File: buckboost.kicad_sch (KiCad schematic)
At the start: 25 parts, among them Q3 DUAL_N_FET, Q4 DUAL_N_FET, U4 LM5176

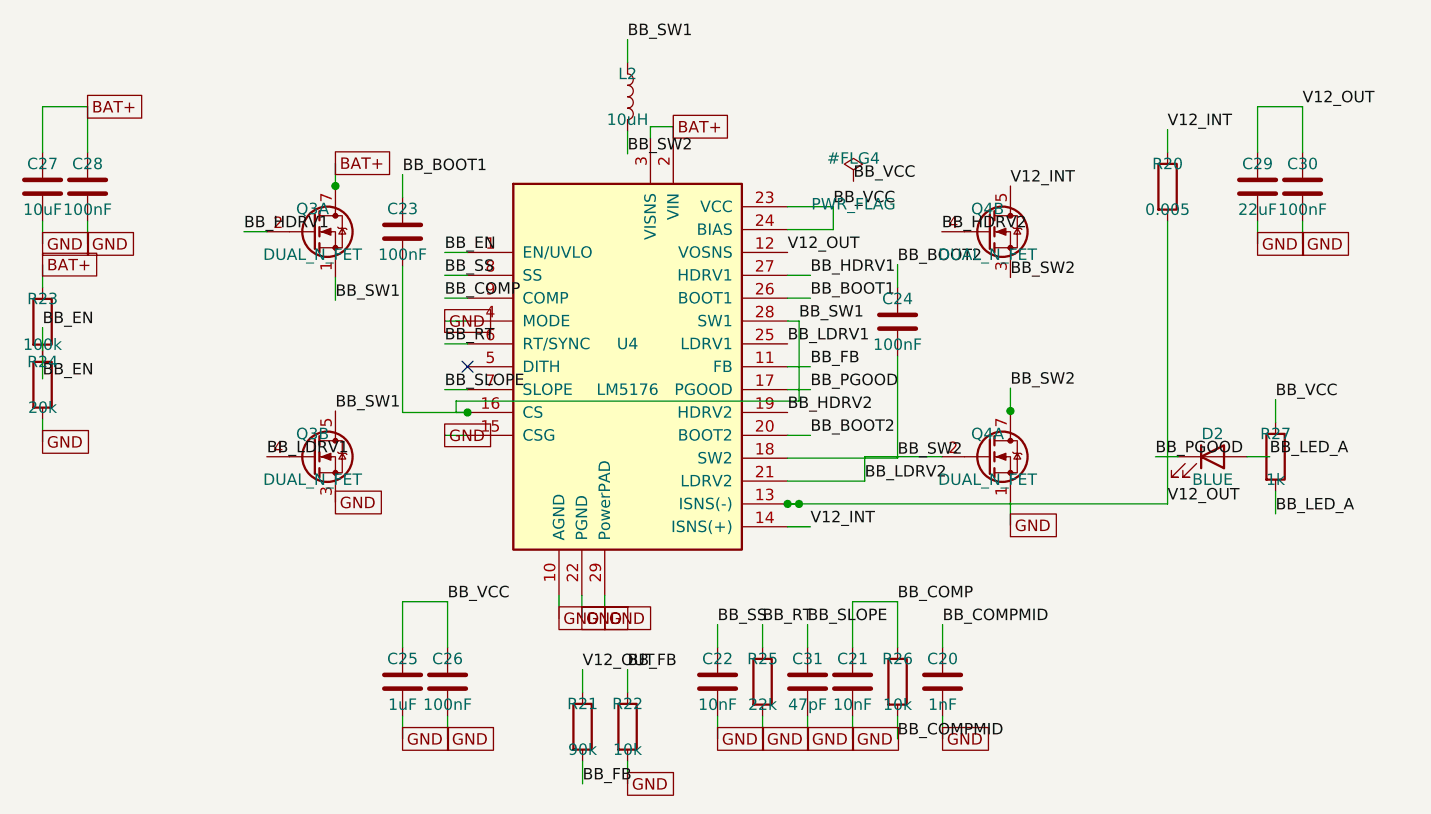
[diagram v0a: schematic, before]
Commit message: schematic: integrate subcircuits — output, I²C, user switch
Top-level power_module.kicad_sch gains the user-facing components:

  J2  Conn_01x02   output header        : V12_OUT, GND
  J3  Conn_01x04   I²C breakout         : SDA, SCL, ALERT, GND
  SW1 SW_SPDT      user on/off switch   : MODULE_EN ↔ BAT+ (pin 3 NC)

For these to span sheets, V12_OUT (Buck-Boost) and SDA/SCL/ALERT (BMS)
were promoted from local labels to global_label inside their child
sheets (one Python pass over each .kicad_sch).  KiCad joins
global_labels by name across all sheets without sheet pins.

User switch behaviour: SW1 routes BAT+ through to a new MODULE_EN
global net.  Inside buckboost.kicad_sch, R23.pin1 (top of the
LM5176 EN/UVLO divider) was switched from BAT+ to MODULE_EN — so
opening SW1 lets R24 pull EN/UVLO low and the buck-boost shuts
down (BMS still runs at its ~10 µA sleep current).

Cleanup: SW1 placeholder in the BMS sheet was deleted (it was
intentionally unwired pending integration; now the real user switch
lives at the parent).

ERC: top-level reports zero errors.  One warning remains
(L_Bourns_SRR1280 footprint not found in default library — pending
the LCSC/footprint-property pass that's still on the to-do list).

Co-Authored-By: Claude Opus 4.7 <noreply@anthropic.com>
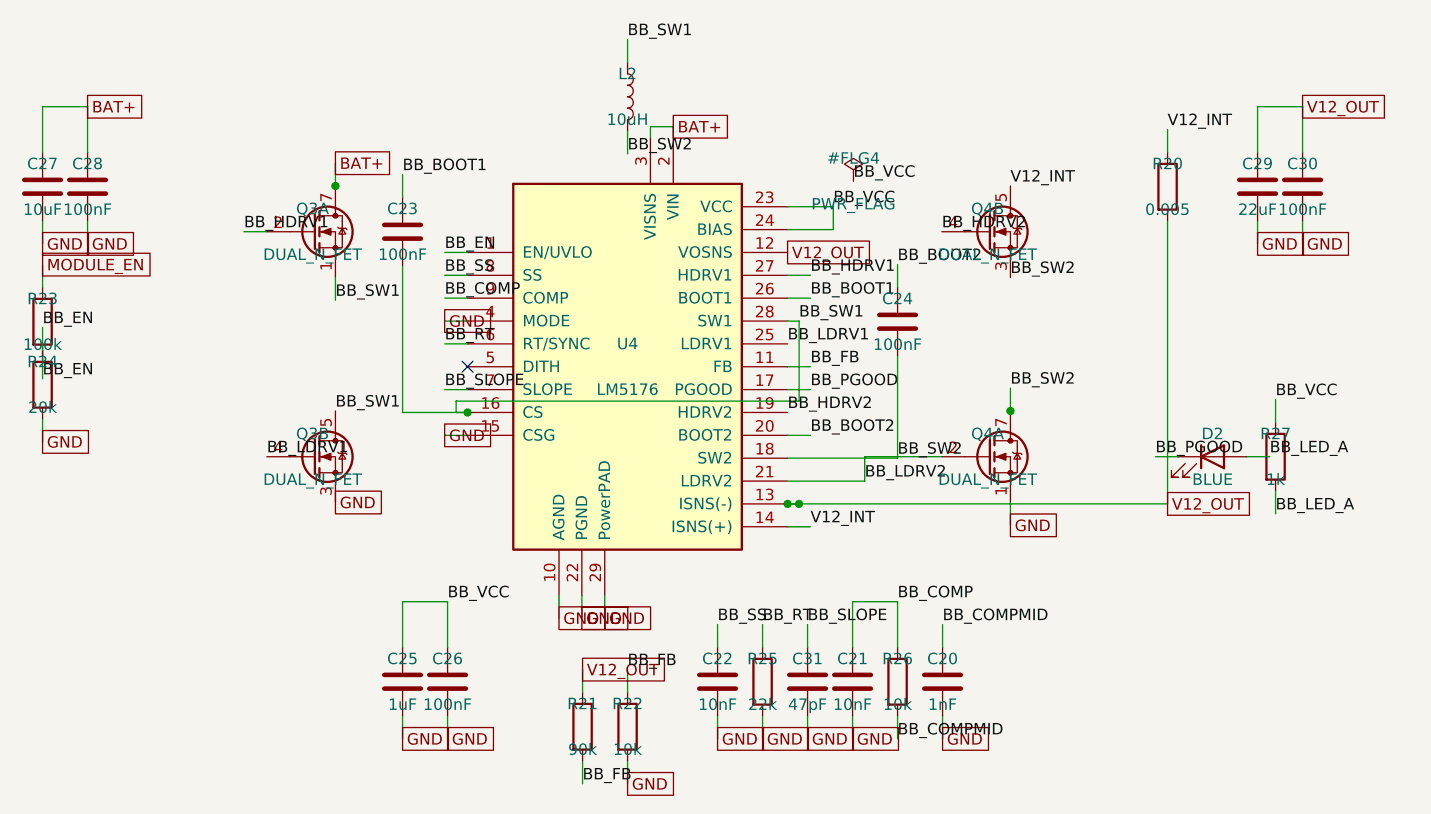
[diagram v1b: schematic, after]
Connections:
- net BAT+: no longer R23.1
- new net MODULE_EN: R23.1
